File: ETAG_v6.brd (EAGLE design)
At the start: 68.6 x 53.3 mm, 94 parts, among them CN2 PINHEAD-2x5-P1.27, IC2 SAMD21G18A-AUT, IC5 RTC_PCF8523T, IC6 EM4095, J1 22-27-2021-02, K1 G3VM-202J1, K2 G3VM-202J1, T1_VDIV P_CHANNEL_MOSFET_, U2 TC7SU04F, Y1 32.768kHz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

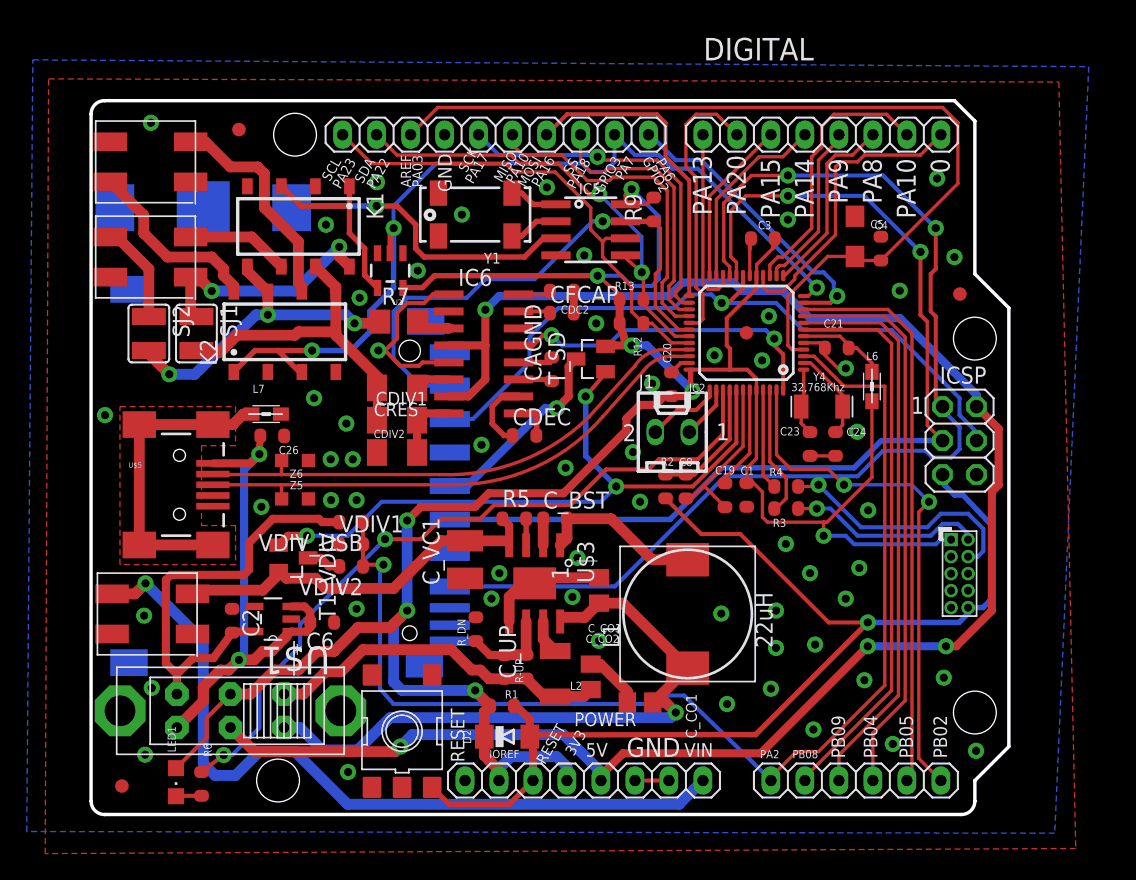
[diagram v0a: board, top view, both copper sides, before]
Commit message: dual level mosfet added to voltage divider
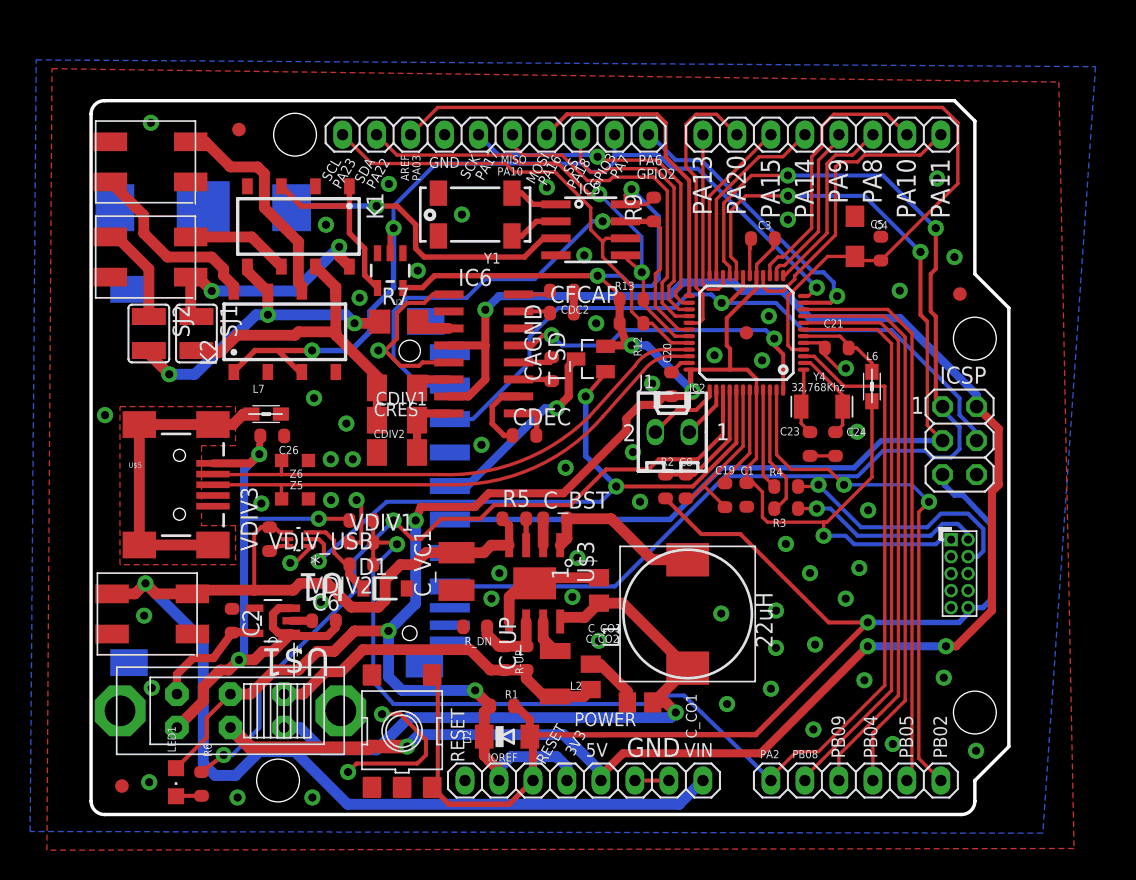
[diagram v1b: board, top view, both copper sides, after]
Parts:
- removed T1_VDIV: P_CHANNEL_MOSFET_, transistor-fet:SOT23
- added D1: (no value), diode:SOD123FL
- added U1: SI1016CX-T1-GE3, Vishay_By_element14_Batch_1:SOT50P162X60-6N
- added VDIV3: 200K, Resistenze:R0603-ROUND
- VDIV1: value ? -> 500K
- VDIV2: value ? -> 1.8M
- moved C_VC1 1.09 mm to (27.3, 18.2)
- moved VDIV1 0.77 mm to (20.2, 20.3)
- moved VDIV2 0.77 mm to (20.2, 18.7)
- moved VDIV_USB 0.77 mm to (20.2, 22.0)
- moved R-UP 0.66 mm to (30.9, 11.7)
- moved C_UP 0.63 mm to (32.5, 11.7)
- moved R_DN 0.18 mm to (28.7, 14.0), turned to 0 degrees
- moved C6 0.18 mm to (17.4, 14.5), turned to 0 degrees
- moved U$1 0.13 mm to (13.6, 14.5)
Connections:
- removed net N$23: T1_VDIV.3, VDIV2.2
- new net N$15: U1.5, U1.6, VDIV3.1
- new net N$21: D1.C, U1.3, VDIV2.2
- net +12V: now also U1.4, VDIV3.2; no longer T1_VDIV.2
- net GND: now also D1.A, U1.1
- net PA28_2FETS: now also U1.2; no longer T1_VDIV.1
- net X3.3V: no longer VDIV_USB.2
- net XUSB: now also VDIV_USB.2
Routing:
- net X3.3V: track 32.5 -> 8.93 mm
- net GND: track 57.2 -> 76.9 mm, vias 58 -> 62
- net XUSB: track 37.5 -> 49.7 mm, vias 2 -> 3
- net +12V: track 89.4 -> 99.6 mm
- net RESET: track 84.4 -> 93.1 mm
- net N$21: track 0.00 -> 6.70 mm
- net PA02_AIN0: track 87.8 -> 90.4 mm
- net N$23: track 2.59 -> 0.00 mm
- net N$15: track 0.00 -> 2.24 mm
- net +3V3: track 186.7 -> 184.8 mm
- net PA27_TX_LED: track 55.4 -> 57.0 mm
- net N$7: track 6.68 -> 5.70 mm
- net PA7_RF_SWTICH: track 67.7 -> 67.1 mm
- net PA28_2FETS: track 51.4 -> 51.9 mm
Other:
- board text added: "PA11"
- board text removed: "0"
- board text removed: "DIGITAL"

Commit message: Design submitted to PCB shop
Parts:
- removed J1: 22-27-2021-02, con-molex:6410-02
- removed R3, R4: 0R, Resistenze:R0603-ROUND
- removed TP_10, TP_12, TP_A0, TP_A1, TP_A2, TP_A3, TP_A4, TP_AREF, TP_MOSI, TP_RESET, TP_SCK, TP_SCL, TP_SDA: TP_SP, SmartPrj:TP-SP
- added JP1: (no value), pinhead:1X02
- added R10, R8: 10k, Resistenze:R0603-ROUND
- added VAR_C: TZB4Z100AB10R00, mylibrary:TZB4Z100AB10R00
- moved L7 9.96 mm to (3.30, 31.8), turned to 180 degrees
- moved CDIV2 5.01 mm to (27.8, 27.8), turned to 0 degrees
- moved R6 2.43 mm to (10.7, 2.54)
- moved LED1 2.01 mm to (8.26, 3.05)
- moved C26 1.40 mm to (12.5, 27.4), turned to 90 degrees
- moved ANT1 0.38 mm to (4.83, 41.7)
- moved ANT2 0.38 mm to (4.83, 48.8)
- moved G1 0.25 mm to (8.64, 45.3)
- moved U$6 0.25 mm to (4.83, 15.0)
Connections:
- removed net PA10_MISO: TP_12.X
- removed net SWCLK: CN2.4, R4.2
- removed net SWDIO: CN2.2, R3.1
- new net N$22: K1.2, K1.4, K2.2, K2.4, R8.2
- net GND: now also R10.1, R8.1; no longer K1.2, K1.4, K2.2, K2.4
- net N$11: now also VAR_C.P$2
- net N$12: now also VAR_C.P$1
- net PA02_AIN0: no longer TP_A0.X
- net PA03_AREFA: no longer TP_AREF.X
- net PA04_AIN4: no longer TP_A3.X
- net PA05_AIN5: no longer TP_A4.X
- net PA16_MOSI: no longer TP_MOSI.X
- net PA17_SCK: no longer TP_SCK.X
- net PA18_SS: no longer TP_10.X
- net PA22_SDA: no longer TP_SDA.X
- net PA23_SCL: no longer TP_SCL.X
- net PA28_2FETS: now also R10.2
- net PA30_SWCLK: now also CN2.4; no longer R4.1
- net PA31_SWDIO: now also CN2.2; no longer R3.2
- net PB08_AIN2: no longer TP_A1.X
- net PB09_AIN3: no longer TP_A2.X
- net PB22_DEBUG_TX: now also JP1.2; no longer J1.2
- net PB23_DEBUG_RX: now also JP1.1; no longer J1.1
- net RESET: no longer TP_RESET.X
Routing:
- net N$22: track 0.00 -> 43.8 mm, vias 0 -> 2
- net PA30_SWCLK: track 7.55 -> 28.3 mm, vias 0 -> 1
- net SWCLK: track 19.0 -> 0.00 mm, vias 1 -> 0
- net SWDIO: track 14.6 -> 0.00 mm, vias 1 -> 0
- net PA31_SWDIO: track 10.1 -> 24.6 mm, vias 0 -> 1
- net N$12: track 2.61 -> 13.2 mm
- net GND: track 76.9 -> 69.9 mm, vias 62 -> 63
- net N$11: track 24.7 -> 31.6 mm
- net VBAT1: track 23.0 -> 26.0 mm
- net +3V3: track 184.8 -> 182.1 mm
- net XUSB: track 49.7 -> 47.7 mm
- net +5_PSU: track 50.1 -> 48.2 mm
- net PB02: track 39.5 -> 40.9 mm
- net PA28_2FETS: track 51.9 -> 53.1 mm
- net PA02_AIN0: track 90.4 -> 89.2 mm
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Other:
- outline, holes or cut-outs redrawn
- board text added: "BAT"
- board text added: "USB"
- board text removed: "ON"
- board text removed: "designed by"
- board text removed: "tinker it"
